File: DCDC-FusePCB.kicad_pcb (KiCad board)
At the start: 2 copper layers, 112.5 x 39 mm, 26 parts, among them J1 Conn_01x02_Socket, J2 Conn_01x02_Socket, J3 Conn_01x02_Socket, J4 Conn_01x02_Socket, J5 Precharge Resistor Breakout, J6 Conn_01x02_Socket, U1 FDP3651U, U2 TCMT1100, U3 FDP3651U

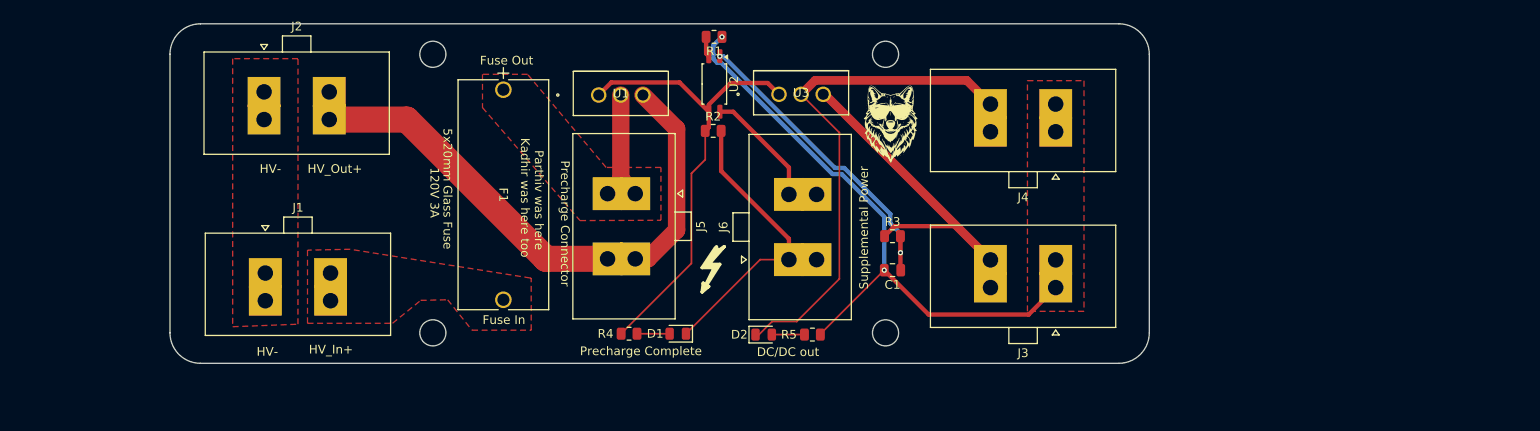
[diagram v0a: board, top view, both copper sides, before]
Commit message: precharge board with resistor
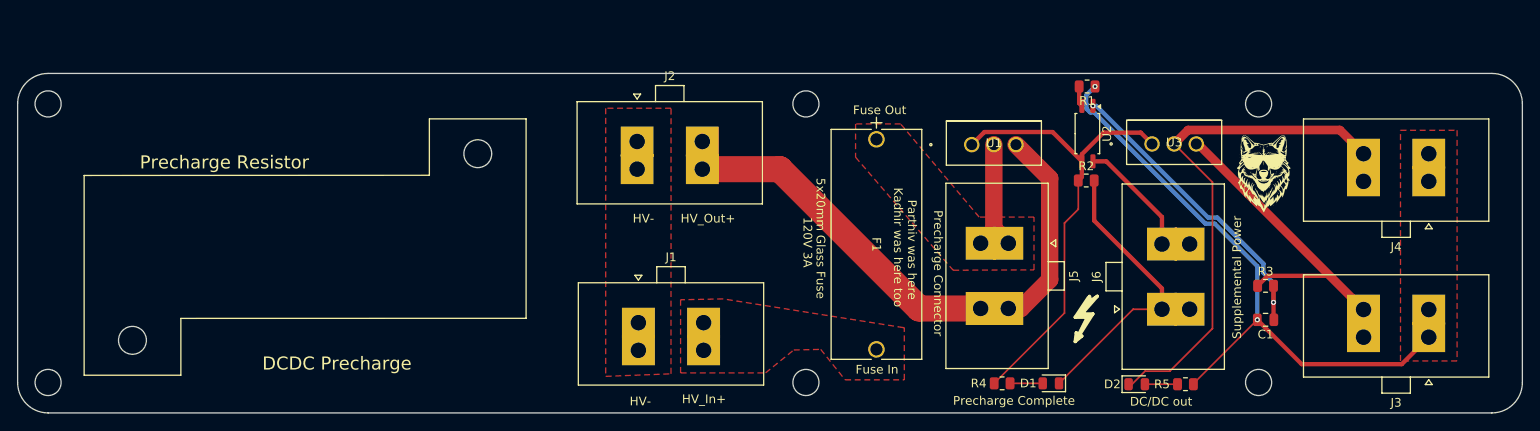
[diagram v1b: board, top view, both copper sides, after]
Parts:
- added REF**: MountingHole_3mm, MountingHole:MountingHole_3mm, F.Cu at (67.8, 108.2)
- added REF**: MountingHole_3mm, MountingHole:MountingHole_3mm, F.Cu at (67.8, 76.2)
- added RH1: MountingHole, MountingHole:MountingHole_3.2mm_M3, F.Cu at (117.2, 81.9)
- added RH2: MountingHole, MountingHole:MountingHole_3.2mm_M3, F.Cu at (77.5, 103.4)
- moved D1 43.2 mm to (183.0, 108.3)
- moved F1 43.2 mm to (163.0, 80.3)
- moved G*** 43.2 mm to (207.5, 84.2)
- moved G*** 43.2 mm to (196.6, 102.3)
- moved G*** 43.2 mm to (176.0, 106.3)
- moved J1 43.2 mm to (135.6, 104.5)
- moved J3 43.2 mm to (226.4, 99.8)
- moved J4 43.2 mm to (226.4, 81.9)
- moved J5 43.2 mm to (174.9, 92.2)
- moved R2 43.2 mm to (187.1, 85.0)
- moved R4 43.2 mm to (177.4, 108.3)
- moved R5 43.2 mm to (198.5, 108.4)
- moved U3 43.2 mm to (194.6, 80.8)
- moved J2 43.2 mm to (135.5, 83.7)
- moved C1 43.2 mm to (207.7, 101.0)
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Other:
- board size 112.5 x 39 mm -> 172.9 x 39 mm
- board text added: "DCDC Precharge"
- board text added: "Precharge Resistor"
